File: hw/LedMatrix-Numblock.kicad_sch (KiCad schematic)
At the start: 42 parts, among them Q2200 DTA114E, Q2201 DTA114E, Q2202 DTA114E, Q2203 DTA114E, Q2204 DTA114E, Q2205 DTA114E, Q2206 DTC114EE, Q2207 DTC114EE, Q2208 DTC114EE, Q2209 DTC114EE, Q2210 DTC114EE, Q2211 DTC114EE, Q2212 DTC114EE, Q2213 DTC114EE, Q2214 DTC114EE

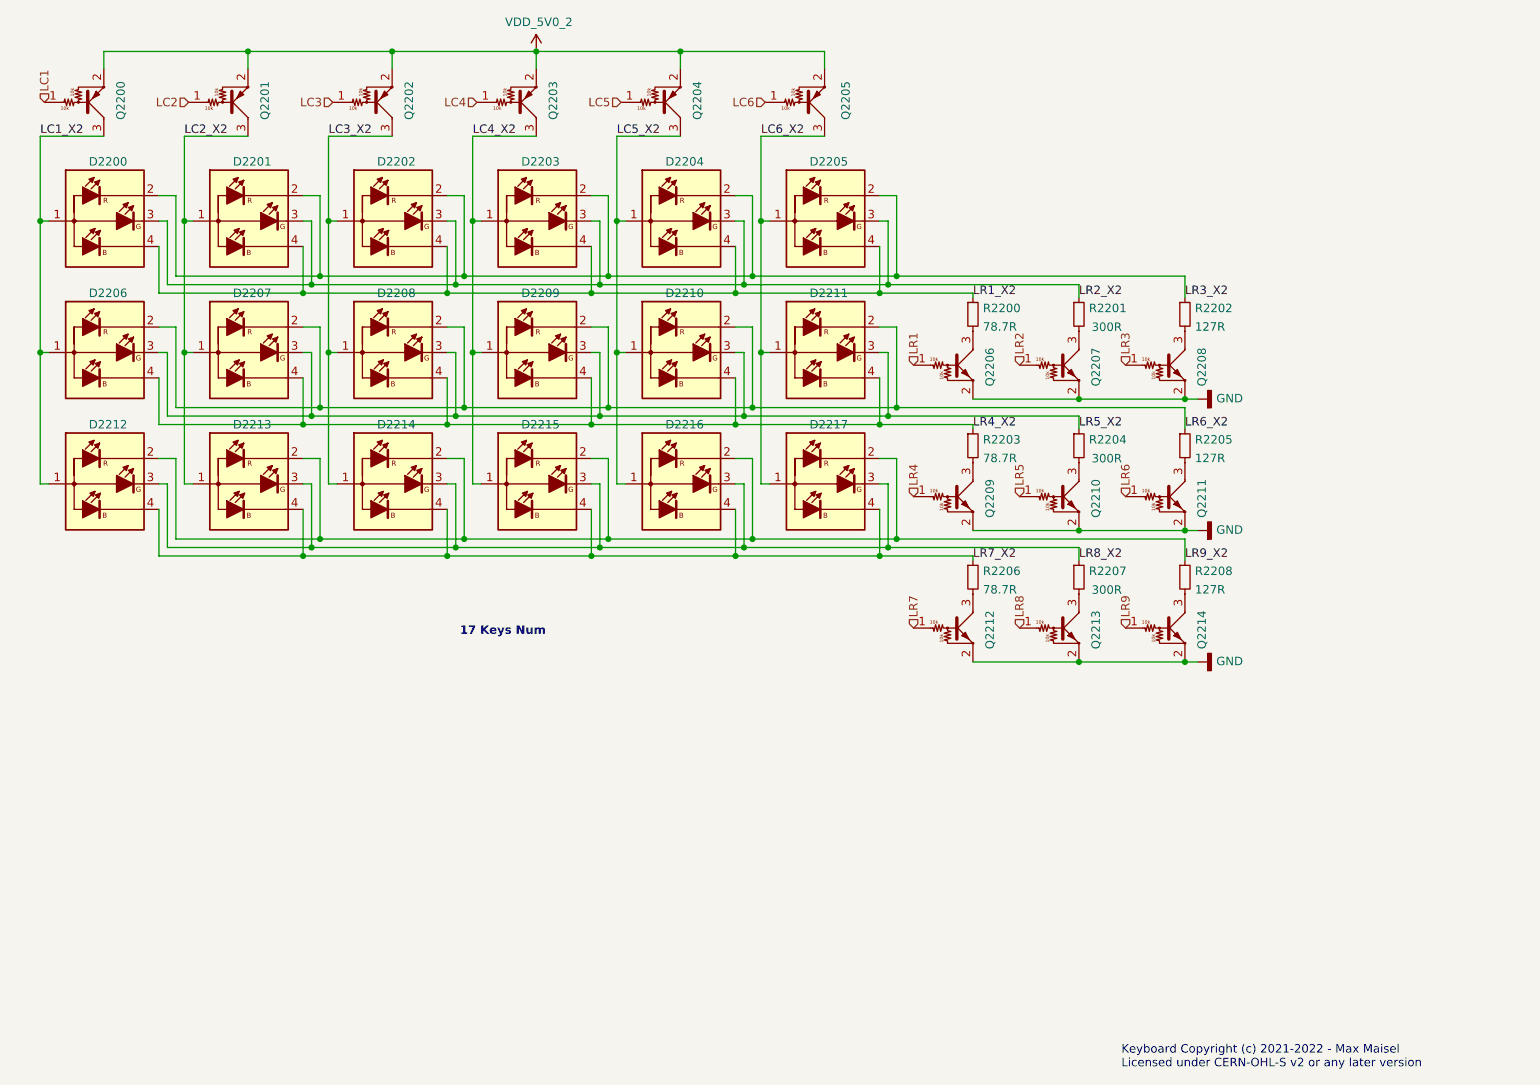
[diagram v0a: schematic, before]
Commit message: Replace LED matrix BJTs with MOSFETs and update PCB.
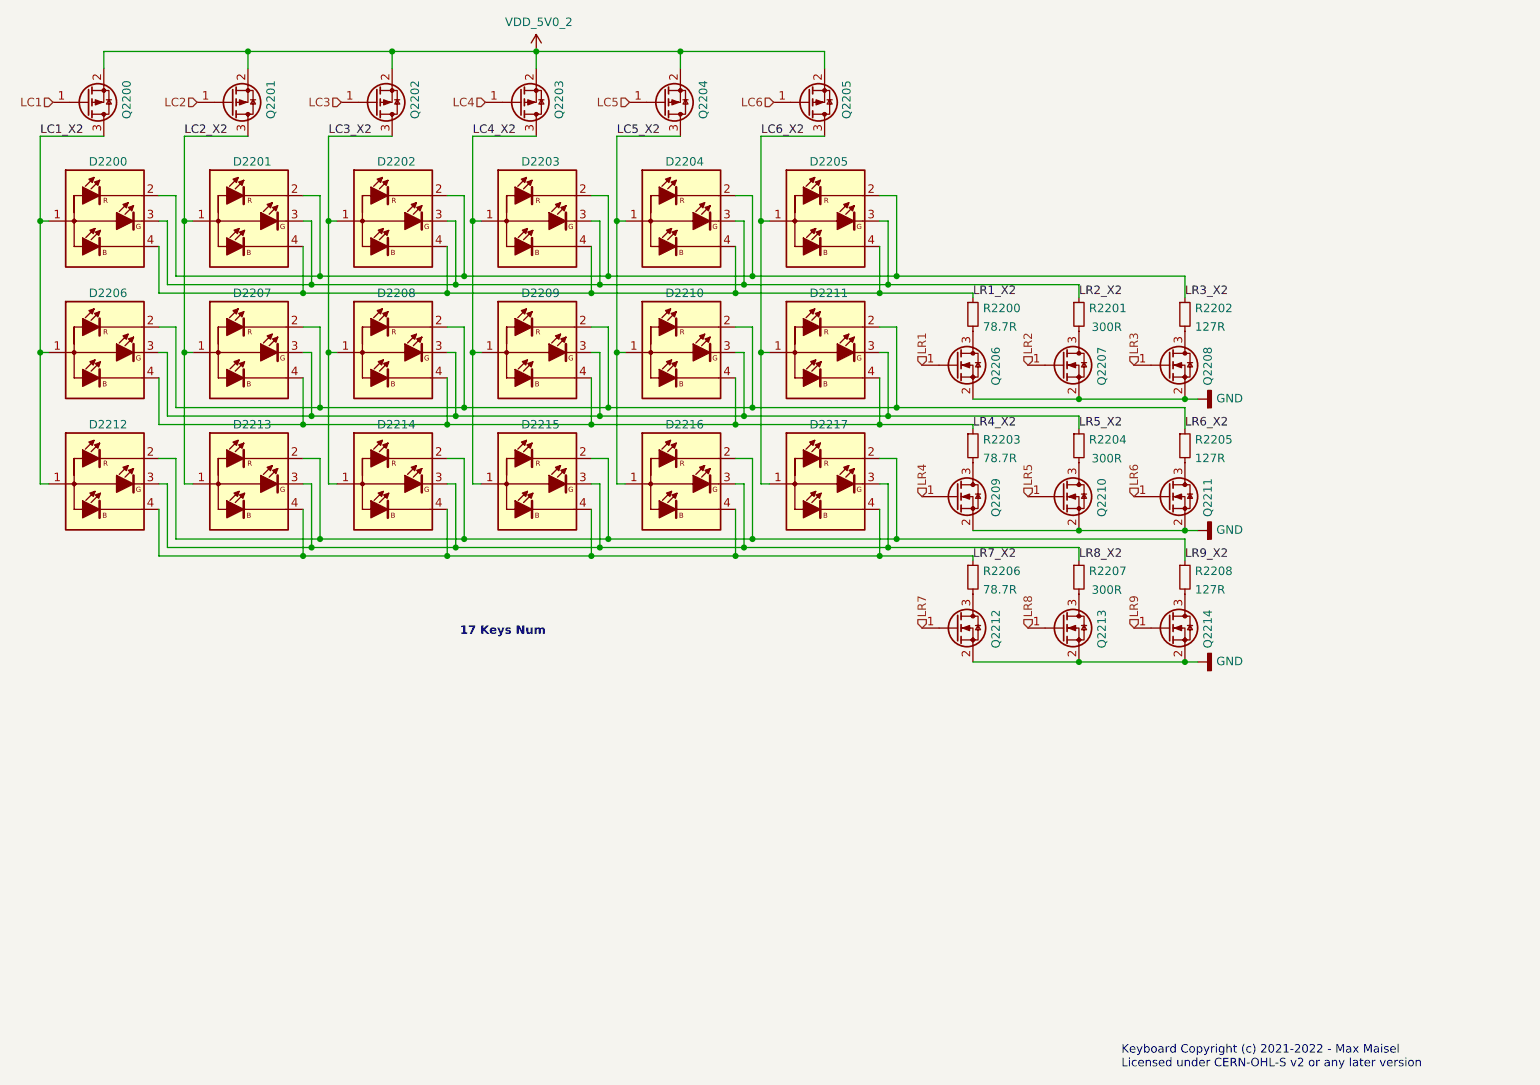
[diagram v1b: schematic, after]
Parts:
- Q2200, Q2201, Q2202, Q2203, Q2204, Q2205: value DTA114E -> NTA4151P; symbol Keyboard:DTA114E -> Keyboard:NTA4151PT1G; farnell# (none) -> 2317622; mouser# (none) -> 863-NTA4151PT1G
- Q2206, Q2207, Q2208, Q2209, Q2210, Q2211, Q2212, Q2213, Q2214: value DTC114EE -> NTA4153N; symbol Keyboard:DTC114EE -> Keyboard:NTA4153NT1G; farnell# (none) -> 2317621; mouser# 863-DTC114EET1G -> 863-NTA4153NT1G
